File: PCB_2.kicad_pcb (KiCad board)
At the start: 2 copper layers, 80 x 50 mm, 19 parts, among them Q3 Q_NPN_BCE, Q4 Q_NPN_BCE, U3 TEA1-0505

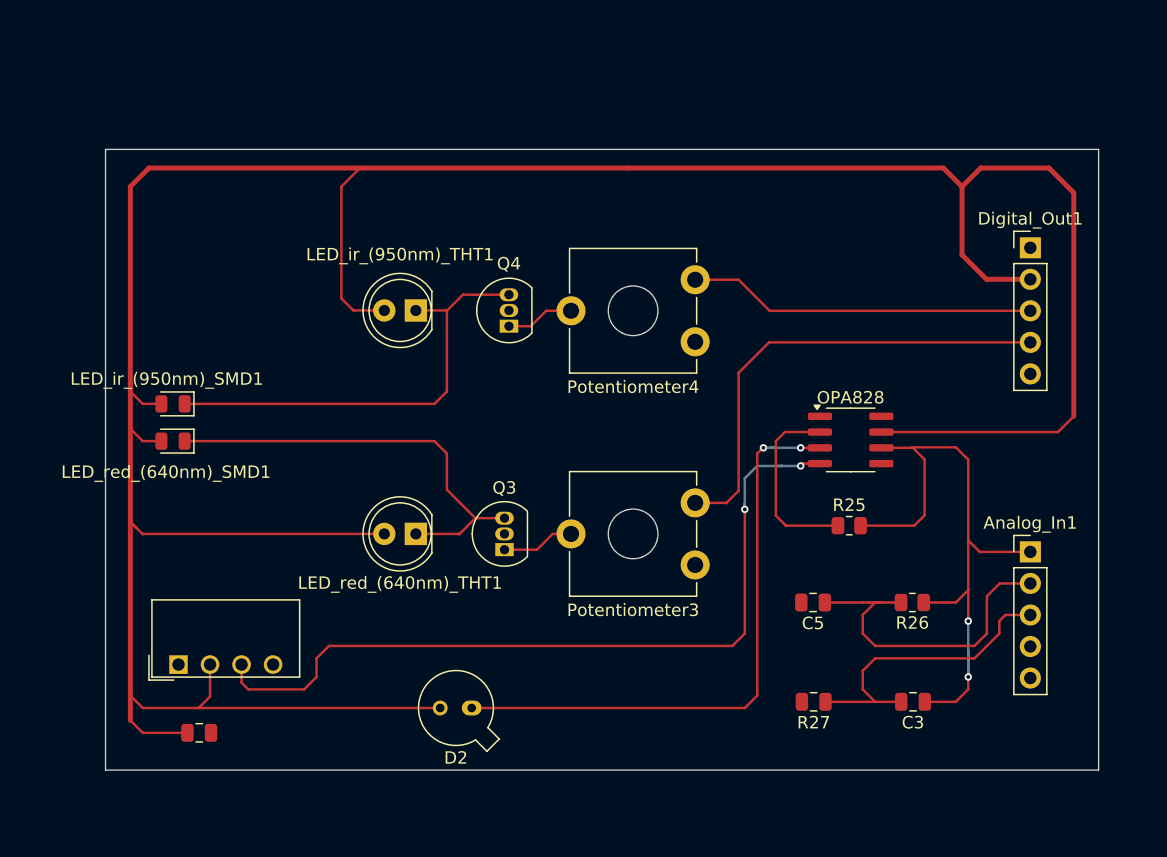
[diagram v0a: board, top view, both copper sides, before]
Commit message: Updated schematic and layout, cleaned backups
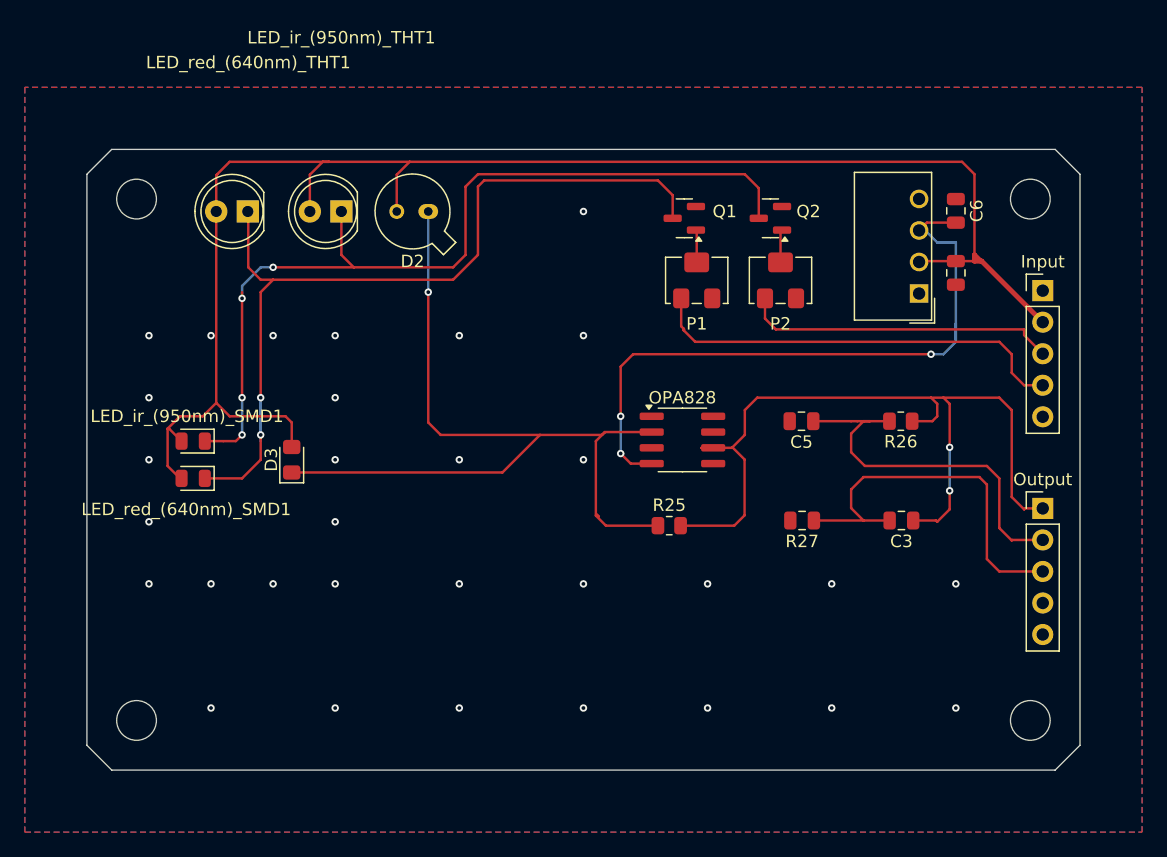
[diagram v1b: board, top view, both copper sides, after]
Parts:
- removed Q3, Q4: Q_NPN_BCE, Package_TO_SOT_THT:TO-92_Inline
- added C6: 10u, Capacitor_SMD:C_0805_2012Metric, F.Cu at (169.0, 76.0)
- added D3: D_Photo, Diode_SMD:D_0805_2012Metric_Pad1.15x1.40mm_HandSolder, F.Cu at (115.5, 96.0)
- added Q1: BC817, Package_TO_SOT_SMD:SOT-23, F.Cu at (147.1, 76.5)
- added Q2: BC817, Package_TO_SOT_SMD:SOT-23, F.Cu at (154.1, 76.5)
- added REF**: MountingHole_3.2mm_M3, MountingHole:MountingHole_3.2mm_M3, F.Cu at (103.0, 75.0)
- added REF**: MountingHole_3.2mm_M3, MountingHole:MountingHole_3.2mm_M3, F.Cu at (175.0, 117.0)
- added REF**: MountingHole_3.2mm_M3, MountingHole:MountingHole_3.2mm_M3, F.Cu at (175.0, 75.0)
- added REF**: MountingHole_3.2mm_M3, MountingHole:MountingHole_3.2mm_M3, F.Cu at (103.0, 117.0)
- C3: value 10 nF -> 10n
- C4: value C_Small -> 10u
- C5: value 10 uF -> 10u
- P1: renamed from Potentiometer3; footprint Potentiometer_THT:Potentiometer_ACP_CA9-V10_Vertical_Hole -> Potentiometer_SMD:Potentiometer_Bourns_3214W_Vertical
- P2: renamed from Potentiometer4; footprint Potentiometer_THT:Potentiometer_ACP_CA9-V10_Vertical_Hole -> Potentiometer_SMD:Potentiometer_Bourns_3214W_Vertical
- R25: value 1 MΩ -> 1M
- R26: value 1000 Ω -> 1k
- moved C4 71.3 mm to (169.0, 81.0), turned to -90 degrees
- moved U3 66.7 mm to (166.0, 82.6), turned to 180 degrees
- moved D2 40.2 mm to (126.5, 76.0)
- moved LED_red_(640nm)_THT1 29.3 mm to (112.0, 76.0)
- moved P1 17.9 mm to (148.1, 81.5)
- moved C3 14.6 mm to (164.6, 100.9)
- moved C5 14.6 mm to (156.6, 92.9)
- moved R26 14.6 mm to (164.6, 92.9)
- moved R27 14.6 mm to (156.6, 100.9)
- moved R25 14.5 mm to (145.9, 101.3)
- moved OPA828 13.6 mm to (147.0, 94.4)
- moved LED_ir_(950nm)_THT1 9.98 mm to (119.5, 76.0)
- moved P2 6.88 mm to (154.9, 81.5)
- moved Output 3.64 mm to (176.0, 99.9)
- moved Input 3.60 mm to (176.0, 82.4)
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- renumbered Digital_Out1 to Input, Analog_In1 to Output
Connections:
- Input pad 5: unconnected-(Digital_Out1-Pin_5-Pad5) -> GND
- OPA828 pad 2: Net-(OPA828--) -> Net-(D2-K)
- OPA828 pad 3: Net-(D2-K) -> GND
- R25 pad 1: Net-(OPA828--) -> Net-(D2-K)
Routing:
- net +5V: track 244.3 -> 129.9 mm
- net Net-(LED_ir_(950nm)_SMD1-K): track 36.1 -> 72.1 mm, vias 0 -> 4
- net Net-(LED_red_(640nm)_SMD1-K): track 35.6 -> 71.5 mm, vias 0 -> 2
- net Net-(D2-K): track 48.8 -> 68.4 mm, vias 2 -> 1
- net Net-(OPA828--): track 15.2 -> 0.00 mm
- net /A_Op_Amp1: track 53.2 -> 66.6 mm
- net -5V: track 65.0 -> 54.0 mm, vias 2 -> 3
- net /A_High_Pass: track 25.0 -> 31.5 mm
- net Net-(Q2-B): track 7.21 -> 2.65 mm
- net Net-(Q1-B): track 6.39 -> 2.63 mm
- net /D_LED_950: track 37.9 -> 34.4 mm
- net /D_LED_640: track 28.5 -> 25.4 mm
- net /A_Low_Pass: track 27.3 -> 30.3 mm
- net GND: vias 0 -> 31
- added copper zone on B.Cu, net GND
- added copper zone on F.Cu, net GND
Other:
- outline, holes or cut-outs redrawn
